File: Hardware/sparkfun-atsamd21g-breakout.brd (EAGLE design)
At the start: 17.8 x 33 mm, 41 parts, among them Q1 2N7002PW, Q3 2.5A/30V, U1 ATSAMD21G-A, U2 MIC5219 3.3V, U3 74AHC1G125, Y1 32.768kHz

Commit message: Swapping MIC5205 Regulator out for AP2112K-3.3V
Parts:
- U2: value MIC5219 3.3V -> 3.3V
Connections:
- net RAW renamed VIN
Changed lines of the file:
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@@
 <attribute name="VALUE" value="15pF" x="7.62" y="7.366" size="1.778" layer="27" rot="R270" display="off"/>
 </element>
-<element name="U2" library="SparkFun-PowerIC" package="SOT23-5" value="MIC5219 3.3V" x="7.62" y="21.209" rot="R180">
-<attribute name="PROD_ID" value="VREG-09872" x="7.62" y="21.209" size="0.889" layer="27" font="vector" ratio="15" rot="R180" display="off"/>
+<element name="U2" library="SparkFun-PowerIC" package="SOT23-5" value="3.3V" x="7.62" y="21.209" rot="R180">
+<attribute name="PROD_ID" value="VREG-12457" x="7.62" y="21.209" size="0.889" layer="27" font="vector" ratio="15" rot="R180" display="off"/>
 </element>
 <element name="D2" library="SparkFun-LED" package="LED-0603" value="RED" x="1.905" y="30.988" rot="R270">
@@
 <wire x1="14.4018" y1="4.1656" x2="13.8684" y2="4.699" width="0.1524" layer="16"/>
 </signal>
-<signal name="RAW">
+<signal name="VIN">
 <contactref element="JP2" pad="1"/>
 <contactref element="U2" pad="1"/>

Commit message: Tweaking schematic and layout silk for checklist
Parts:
- moved FRAME1 2.54 mm to (-12.7, -19.1)
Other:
- board text added: "Units in inches"
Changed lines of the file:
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@@
 <text x="14.4018" y="30.988" size="0.8128" layer="21" font="vector" ratio="15" rot="R90" align="bottom-center">13</text>
 <text x="3.3782" y="30.988" size="0.8128" layer="21" font="vector" ratio="15" rot="R270" align="bottom-center">PWR</text>
-<text x="17.78" y="-16.51" size="1.778" layer="51" font="vector" ratio="15">Jim Lindblom</text>
-<dimension x1="0" y1="0" x2="0" y2="33.02" x3="-6.35" y3="16.51" textsize="1.27" textratio="15" layer="47" dtype="vertical" unit="inch"/>
-<dimension x1="0" y1="0" x2="17.78" y2="0" x3="8.89" y3="-7.62" textsize="1.27" textratio="15" layer="47" dtype="horizontal" unit="inch"/>
-<dimension x1="0" y1="0" x2="1.27" y2="1.27" x3="0.635" y3="-2.54" textsize="1.27" textratio="15" layer="47" dtype="horizontal" unit="inch"/>
-<dimension x1="0" y1="0" x2="16.51" y2="1.27" x3="8.255" y3="-5.08" textsize="1.27" textratio="15" layer="47" dtype="horizontal" unit="inch"/>
-<dimension x1="0" y1="0" x2="1.27" y2="1.27" x3="-1.27" y3="0.635" textsize="1.27" textratio="15" layer="47" dtype="vertical" unit="inch"/>
-<dimension x1="0" y1="0" x2="1.27" y2="3.81" x3="-3.81" y3="1.905" textsize="1.27" textratio="15" layer="47" dtype="vertical" unit="inch"/>
+<text x="17.78" y="-19.05" size="1.778" layer="51" font="vector" ratio="15">Jim Lindblom</text>
+<dimension x1="0" y1="0" x2="0" y2="33.02" x3="-10.16" y3="16.51" textsize="1.27" textratio="15" layer="47" dtype="vertical" unit="inch" precision="3"/>
+<dimension x1="0" y1="0" x2="17.78" y2="0" x3="8.89" y3="-10.16" textsize="1.27" textratio="15" layer="47" dtype="horizontal" unit="inch" precision="3"/>
+<dimension x1="0" y1="0" x2="1.27" y2="1.27" x3="0.635" y3="-2.54" textsize="1.27" textratio="15" layer="47" dtype="horizontal" unit="inch" precision="3"/>
+<dimension x1="0" y1="0" x2="16.51" y2="1.27" x3="8.255" y3="-7.62" textsize="1.27" textratio="15" layer="47" dtype="horizontal" unit="inch" precision="3"/>
+<dimension x1="0" y1="0" x2="1.27" y2="1.27" x3="-1.27" y3="0.635" textsize="1.27" textratio="15" layer="47" dtype="vertical" unit="inch" precision="3"/>
+<dimension x1="0" y1="0" x2="1.27" y2="3.81" x3="-3.81" y3="1.905" textsize="1.27" textratio="15" layer="47" dtype="vertical" unit="inch" precision="3"/>
 <text x="8.89" y="32.766" size="1.016" layer="16" font="vector" ratio="15" rot="MR0" align="top-center">v10</text>
 <text x="8.89" y="35.56" size="0.889" layer="51" font="vector" ratio="15" align="bottom-center">This is a 4-layer board!</text>
 <text x="15.4559" y="3.9624" size="0.889" layer="21" font="vector" ratio="15" rot="R90" align="bottom-center">11</text>
+<dimension x1="0" y1="0" x2="13.589" y2="17.907" x3="-6.35" y3="8.9535" textsize="1.27" textratio="15" layer="47" dtype="vertical" unit="inch" precision="3"/>
+<dimension x1="0" y1="0" x2="13.589" y2="17.907" x3="6.7945" y3="-5.08" textsize="1.27" textratio="15" layer="47" dtype="horizontal" unit="inch" precision="3"/>
+<text x="-17.78" y="-7.62" size="1.27" layer="47" font="vector" ratio="15">Units in inches</text>
 </plain>
 <attributes>
@@
 <element name="LOGO2" library="SparkFun-Aesthetics" package="OSHW-LOGO-S" value="OSHW-LOGOS" x="5.334" y="17.6276" rot="MR90"/>
 <element name="LOGO3" library="SparkFun-Aesthetics" package="SFE_LOGO_NAME_FLAME_.1" value="SFE_LOGO_NAME_FLAME.1_INCH" x="7.2136" y="5.9436" rot="MR90"/>
-<element name="FRAME1" library="SparkFun-Aesthetics" package="CREATIVE_COMMONS" value="FRAME-LETTER" x="-12.7" y="-16.51"/>
+<element name="FRAME1" library="SparkFun-Aesthetics" package="CREATIVE_COMMONS" value="FRAME-LETTER" x="-12.7" y="-19.05"/>
 <element name="SJ1" library="SparkFun-Passives" package="PAD-JUMPER-2-NC_BY_TRACE_NO_SILK" value="PWR-LED" x="1.905" y="31.623" rot="MR0"/>
 <element name="S2" library="samd21-temp" package="TACTILE_SWITCH_SMD_4.6X2.8MM" value="RESET" x="8.89" y="1.397" rot="R180">
@@
 <contactref element="U1" pad="2"/>
 <wire x1="7.62" y1="7.946" x2="7.311" y2="7.946" width="0.1524" layer="1"/>
-<wire x1="7.311" y1="7.946" x2="6.731" y2="7.366" width="0.1524" layer="1"/>
 <wire x1="6.64" y1="9.466" x2="6.64" y2="8.672" width="0.1524" layer="1"/>
 <wire x1="6.203" y1="7.366" x2="6.203" y2="8.235" width="0.1524" layer="1"/>
 <wire x1="6.203" y1="8.235" x2="6.64" y2="8.672" width="0.1524" layer="1"/>
 <wire x1="6.731" y1="7.366" x2="6.203" y2="7.366" width="0.1524" layer="1"/>
+<wire x1="7.311" y1="7.946" x2="6.731" y2="7.366" width="0.1524" layer="1"/>
 </signal>
 <signal name="!RESET">

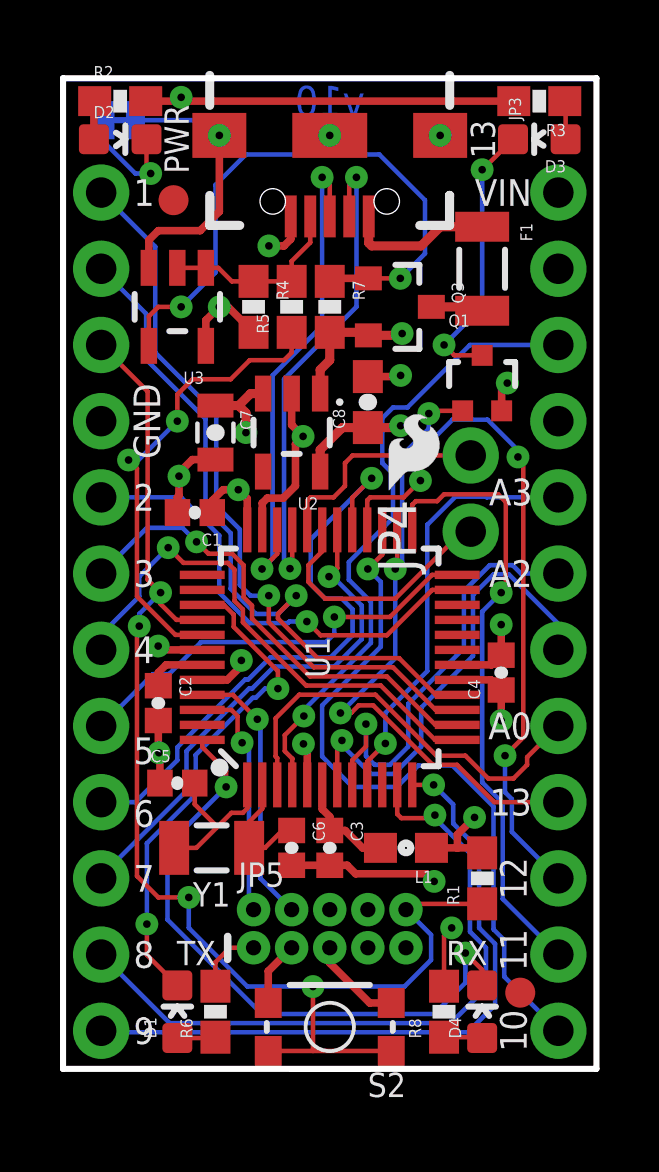
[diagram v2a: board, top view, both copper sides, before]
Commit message: Sequentiallizing part names
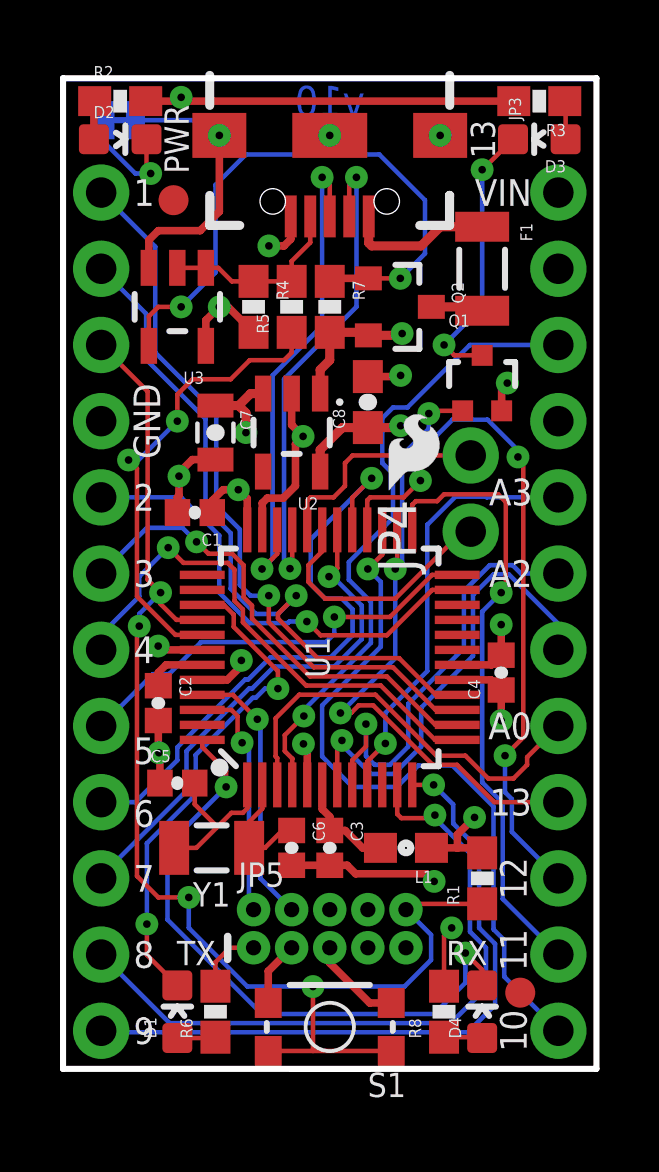
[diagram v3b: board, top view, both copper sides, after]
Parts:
- renumbered Q3 to Q2, S2 to S1
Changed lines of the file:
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@@
 <attribute name="PROD_ID" value="RES-00818" x="7.62" y="25.4" size="0.889" layer="27" font="vector" ratio="15" rot="R90" display="off"/>
 </element>
-<element name="Q3" library="SparkFun-DiscreteSemi" package="SOT23-3" value="2.5A/30V" x="11.176" y="25.4" rot="R270">
+<element name="Q2" library="SparkFun-DiscreteSemi" package="SOT23-3" value="2.5A/30V" x="11.176" y="25.4" rot="R270">
 <attribute name="PROD_ID" value="TRANS-11308" x="11.176" y="25.4" size="0.889" layer="27" font="vector" ratio="15" rot="R270" display="off"/>
 <attribute name="VALUE" value="2.5A/30V" x="11.176" y="25.4" size="1.778" layer="27" rot="R270" display="off"/>
@@
 <element name="FRAME1" library="SparkFun-Aesthetics" package="CREATIVE_COMMONS" value="FRAME-LETTER" x="-12.7" y="-19.05"/>
 <element name="SJ1" library="SparkFun-Passives" package="PAD-JUMPER-2-NC_BY_TRACE_NO_SILK" value="PWR-LED" x="1.905" y="31.623" rot="MR0"/>
-<element name="S2" library="samd21-temp" package="TACTILE_SWITCH_SMD_4.6X2.8MM" value="RESET" x="8.89" y="1.397" rot="R180">
+<element name="S1" library="samd21-temp" package="TACTILE_SWITCH_SMD_4.6X2.8MM" value="RESET" x="8.89" y="1.397" rot="R180">
 <attribute name="PROD_ID" value="SWCH-13065" x="8.89" y="1.397" size="1.778" layer="27" rot="R180" display="off"/>
 </element>
@@
 <wire x1="2.413" y1="31.623" x2="4.702" y2="31.623" width="0.1524" layer="16"/>
 <wire x1="4.702" y1="31.623" x2="5.21" y2="31.115" width="0.1524" layer="16"/>
-<contactref element="S2" pad="2"/>
-<contactref element="S2" pad="1"/>
+<contactref element="S1" pad="2"/>
+<contactref element="S1" pad="1"/>
 <wire x1="6.84" y1="2.197" x2="6.84" y2="3.257" width="0.254" layer="1"/>
 <wire x1="10.94" y1="2.197" x2="10.222" y2="2.197" width="0.254" layer="1"/>
@@
 <wire x1="6.1468" y1="2.7432" x2="8.3312" y2="2.7432" width="0.1524" layer="16"/>
 <wire x1="11.3792" y1="2.7432" x2="12.2682" y2="3.6322" width="0.1524" layer="16"/>
-<contactref element="S2" pad="3"/>
-<contactref element="S2" pad="4"/>
+<contactref element="S1" pad="3"/>
+<contactref element="S1" pad="4"/>
 <wire x1="11.3792" y1="2.7432" x2="8.3312" y2="2.7432" width="0.1524" layer="16"/>
 <wire x1="8.3312" y1="2.7432" x2="8.3312" y2="0.597" width="0.1524" layer="1"/>
@@
 <contactref element="U2" pad="3"/>
 <contactref element="C7" pad="1"/>
-<contactref element="Q3" pad="2"/>
+<contactref element="Q2" pad="2"/>
 <contactref element="R7" pad="2"/>
 <wire x1="8.57" y1="22.5091" x2="8.57" y2="23.302" width="0.3048" layer="1"/>
@@
 <signal name="N$7">
 <contactref element="F1" pad="2"/>
-<contactref element="Q3" pad="3"/>
+<contactref element="Q2" pad="3"/>
 <wire x1="12.276" y1="25.4" x2="13.84" y2="25.4" width="0.3048" layer="1"/>
 <wire x1="13.84" y1="25.4" x2="13.97" y2="25.27" width="0.254" layer="1"/>
@@
 <signal name="N$9">
 <contactref element="U3" pad="4"/>
-<contactref element="Q3" pad="1"/>
+<contactref element="Q2" pad="1"/>
 <contactref element="R7" pad="1"/>
 <wire x1="2.86" y1="24.0999" x2="2.86" y2="25.085" width="0.1524" layer="1"/>
